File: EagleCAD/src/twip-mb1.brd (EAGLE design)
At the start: 81 x 88.9 mm, 13 parts, among them U1 GY-521MPU6050

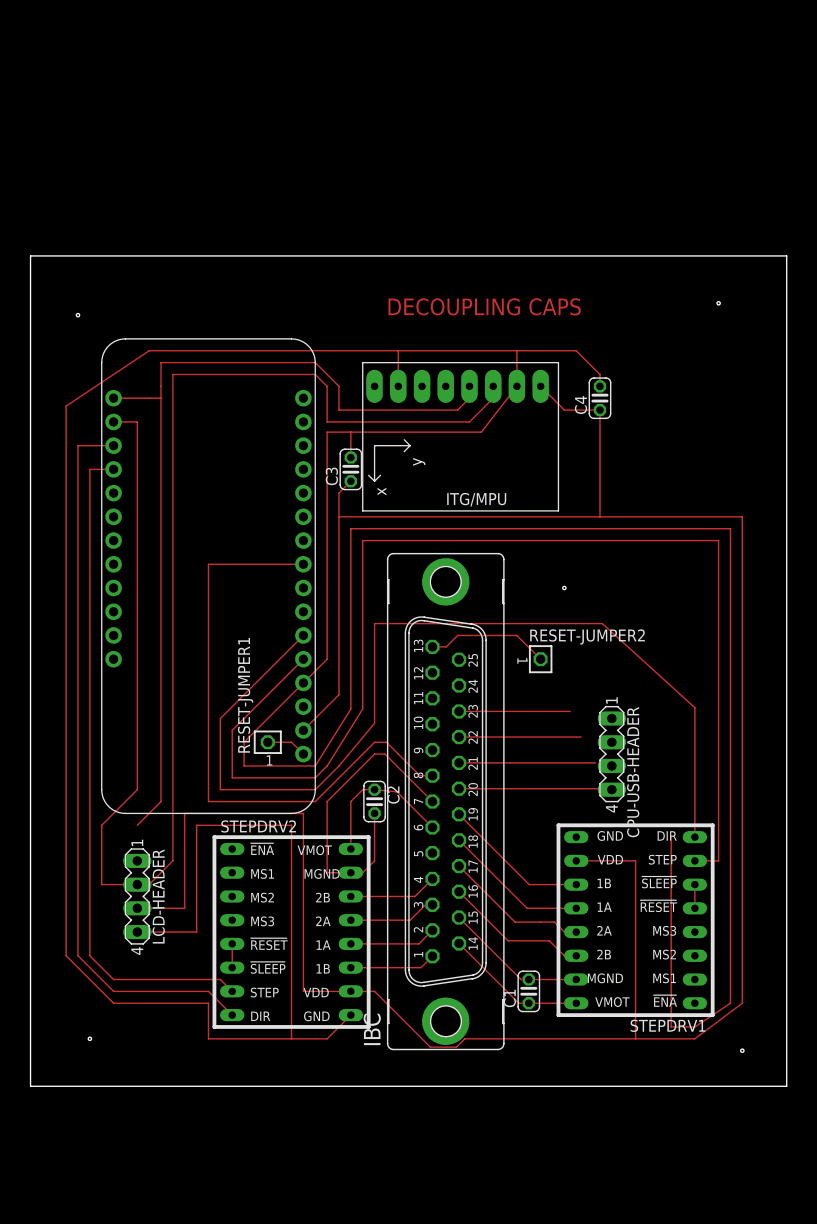
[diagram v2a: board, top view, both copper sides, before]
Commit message: minor layout fixes
need to use version numbers built into copper plate.
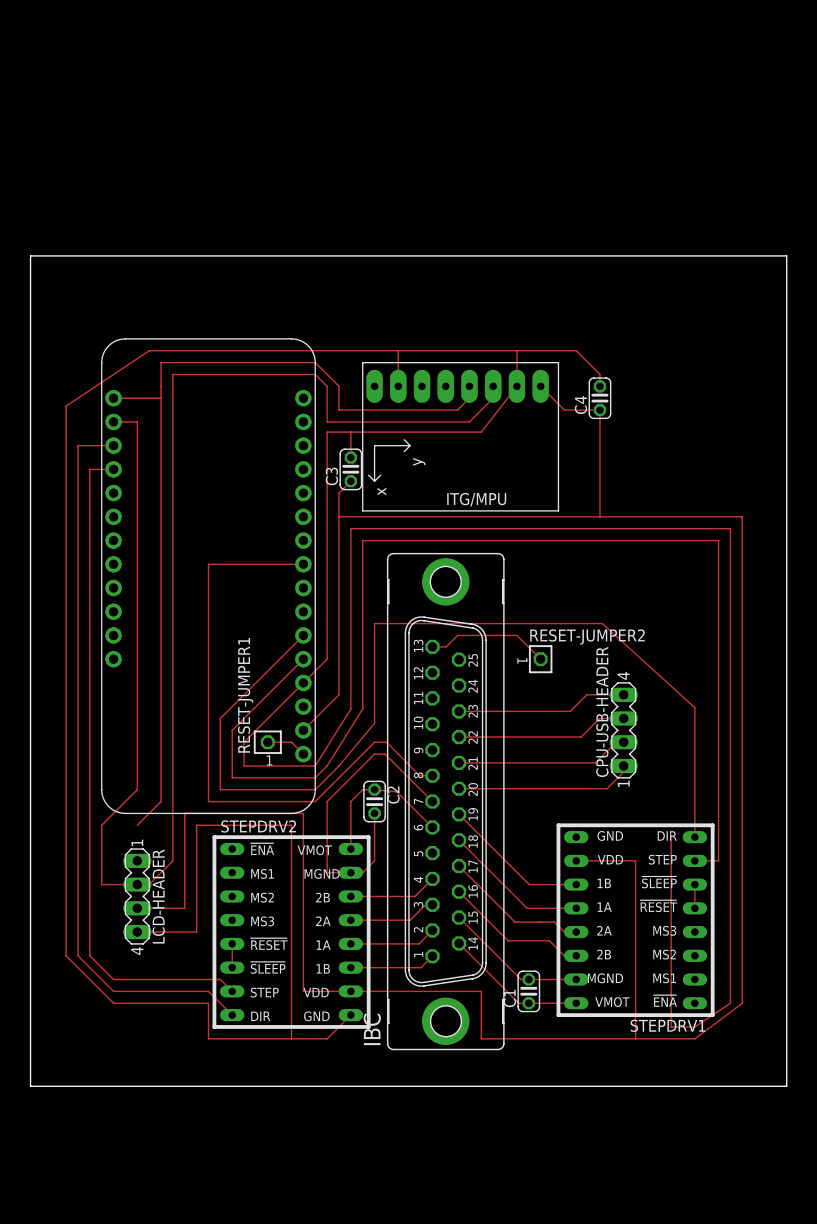
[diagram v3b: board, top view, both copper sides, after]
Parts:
- moved CPU-USB-HEADER 2.84 mm to (69.8, 38.1), turned to 90 degrees
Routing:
- net N$13: track 11.9 -> 18.4 mm
- net N$14: track 13.1 -> 18.4 mm
- net N$18: track 14.6 -> 18.5 mm
- net N$30: track 15.8 -> 19.0 mm
- net 3V: track 266.3 -> 268.6 mm
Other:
- board text removed: "DECOUPLING CAPS"
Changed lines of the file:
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@@
 <dimension x1="0" y1="0" x2="0" y2="88.9" x3="1.27" y3="44.45" textsize="1.778" layer="1" dtype="horizontal" unit="inch"/>
 <dimension x1="6.35" y1="-3.81" x2="87.63" y2="-5.08" x3="46.99" y3="-6.35" textsize="1.778" layer="1" dtype="horizontal" unit="inch"/>
-<hole x="11.43" y="82.55" drill="0.35"/>
-<hole x="80.01" y="83.82" drill="0.35"/>
-<hole x="63.5" y="53.34" drill="0.35"/>
-<hole x="12.7" y="5.08" drill="0.35"/>
-<hole x="82.55" y="3.81" drill="0.35"/>
-<text x="44.45" y="82.55" size="1.778" layer="1">DECOUPLING CAPS</text>
 </plain>
 <attributes>
@@
 <attribute name="SPICEPREFIX" value="C" x="43.18" y="30.48" size="1.778" layer="27" rot="R270" display="off"/>
 </element>
-<element name="CPU-USB-HEADER" library="con-lstb" library_urn="urn:adsk.eagle:library:162" package="MA04-1" package3d_urn="urn:adsk.eagle:package:8337/1" value="" x="68.58" y="35.56" rot="R270">
-<attribute name="MF" value="" x="68.58" y="35.56" size="1.778" layer="27" rot="R270" display="off"/>
-<attribute name="MPN" value="" x="68.58" y="35.56" size="1.778" layer="27" rot="R270" display="off"/>
-<attribute name="OC_FARNELL" value="unknown" x="68.58" y="35.56" size="1.778" layer="27" rot="R270" display="off"/>
-<attribute name="OC_NEWARK" value="unknown" x="68.58" y="35.56" size="1.778" layer="27" rot="R270" display="off"/>
+<element name="CPU-USB-HEADER" library="con-lstb" library_urn="urn:adsk.eagle:library:162" package="MA04-1" package3d_urn="urn:adsk.eagle:package:8337/1" value="" x="69.85" y="38.1" rot="R90">
+<attribute name="MF" value="" x="69.85" y="38.1" size="1.778" layer="27" rot="R90" display="off"/>
+<attribute name="MPN" value="" x="69.85" y="38.1" size="1.778" layer="27" rot="R90" display="off"/>
+<attribute name="OC_FARNELL" value="unknown" x="69.85" y="38.1" size="1.778" layer="27" rot="R90" display="off"/>
+<attribute name="OC_NEWARK" value="unknown" x="69.85" y="38.1" size="1.778" layer="27" rot="R90" display="off"/>
 </element>
 <element name="LCD-HEADER" library="con-lstb" library_urn="urn:adsk.eagle:library:162" package="MA04-1" package3d_urn="urn:adsk.eagle:package:8337/1" value="" x="17.78" y="20.32" rot="R270">
@@
 <wire x1="52.2224" y1="40.132" x2="64.124540625" y2="40.132" width="0.1524" layer="1"/>
 <contactref element="CPU-USB-HEADER" pad="4"/>
-<wire x1="64.124540625" y1="40.132" x2="68.58" y2="31.75" width="0" layer="19" extent="1-1"/>
+<wire x1="64.124540625" y1="40.132" x2="65.902540625" y2="41.91" width="0.1524" layer="1"/>
+<wire x1="65.902540625" y1="41.91" x2="69.85" y2="41.91" width="0.1524" layer="1"/>
 </signal>
 <signal name="N$14">
@@
 <wire x1="52.2224" y1="37.3888" x2="65.30254375" y2="37.3888" width="0.1524" layer="1"/>
 <contactref element="CPU-USB-HEADER" pad="3"/>
-<wire x1="65.30254375" y1="37.3888" x2="68.58" y2="34.29" width="0" layer="19" extent="1-1"/>
+<wire x1="65.30254375" y1="37.3888" x2="67.28374375" y2="39.37" width="0.1524" layer="1"/>
+<wire x1="67.28374375" y1="39.37" x2="69.85" y2="39.37" width="0.1524" layer="1"/>
 </signal>
 <signal name="N$18">
@@
 <wire x1="52.2224" y1="34.6202" x2="66.82481875" y2="34.6202" width="0.1524" layer="1"/>
 <contactref element="CPU-USB-HEADER" pad="2"/>
-<wire x1="66.82481875" y1="34.6202" x2="68.58" y2="36.83" width="0" layer="19" extent="1-1"/>
+<wire x1="66.82481875" y1="34.6202" x2="69.03461875" y2="36.83" width="0.1524" layer="1"/>
+<wire x1="69.03461875" y1="36.83" x2="69.85" y2="36.83" width="0.1524" layer="1"/>
 </signal>
 <signal name="N$30">
@@
 <wire x1="52.2224" y1="31.8516" x2="68.06474375" y2="31.8516" width="0.1524" layer="1"/>
 <contactref element="CPU-USB-HEADER" pad="1"/>
-<wire x1="68.06474375" y1="31.8516" x2="68.58" y2="39.37" width="0" layer="19" extent="1-1"/>
+<wire x1="68.06474375" y1="31.8516" x2="69.85" y2="33.63685625" width="0.1524" layer="1"/>
+<wire x1="69.85" y1="33.63685625" x2="69.85" y2="34.29" width="0.1524" layer="1"/>
 </signal>
 <signal name="N$35">
@@
 <wire x1="64.77" y1="24.13" x2="71.12" y2="24.13" width="0.1524" layer="1"/>
 <wire x1="77.47" y1="5.08" x2="71.12" y2="5.08" width="0.1524" layer="1"/>
-<wire x1="43.18" y1="10.16" x2="40.64" y2="10.16" width="0.1524" layer="1"/>
 <wire x1="39.37" y1="60.96" x2="67.31" y2="60.96" width="0.1524" layer="1"/>
 <wire x1="67.31" y1="60.96" x2="82.55" y2="60.96" width="0.1524" layer="1"/>
 <wire x1="77.47" y1="5.08" x2="82.55" y2="8.89" width="0.1524" layer="1"/>
 <wire x1="71.12" y1="24.13" x2="71.12" y2="5.08" width="0.1524" layer="1"/>
-<wire x1="71.12" y1="5.08" x2="52.83579375" y2="5.08" width="0.1524" layer="1"/>
-<wire x1="52.83579375" y1="5.08" x2="51.94679375" y2="4.191" width="0.1524" layer="1"/>
-<wire x1="51.94679375" y1="4.191" x2="49.149" y2="4.191" width="0.1524" layer="1"/>
-<wire x1="49.149" y1="4.191" x2="43.18" y2="10.16" width="0.1524" layer="1"/>
+<wire x1="71.12" y1="5.08" x2="54.61" y2="5.08" width="0.1524" layer="1"/>
 <contactref element="LCD-HEADER" pad="3"/>
 <wire x1="17.78" y1="19.05" x2="22.86" y2="19.05" width="0.1524" layer="1"/>
@@
 <wire x1="40.64" y1="64.77" x2="39.37" y2="63.5" width="0.1524" layer="1"/>
 <wire x1="39.37" y1="63.5" x2="39.37" y2="60.96" width="0.1524" layer="1"/>
+<wire x1="54.61" y1="10.16" x2="54.61" y2="5.08" width="0.1524" layer="1"/>
+<wire x1="40.64" y1="10.16" x2="54.61" y2="10.16" width="0.1524" layer="1"/>
 </signal>
 <signal name="N$1">

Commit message: minor fixes, and upsized boards to 3.3 x 5 inches
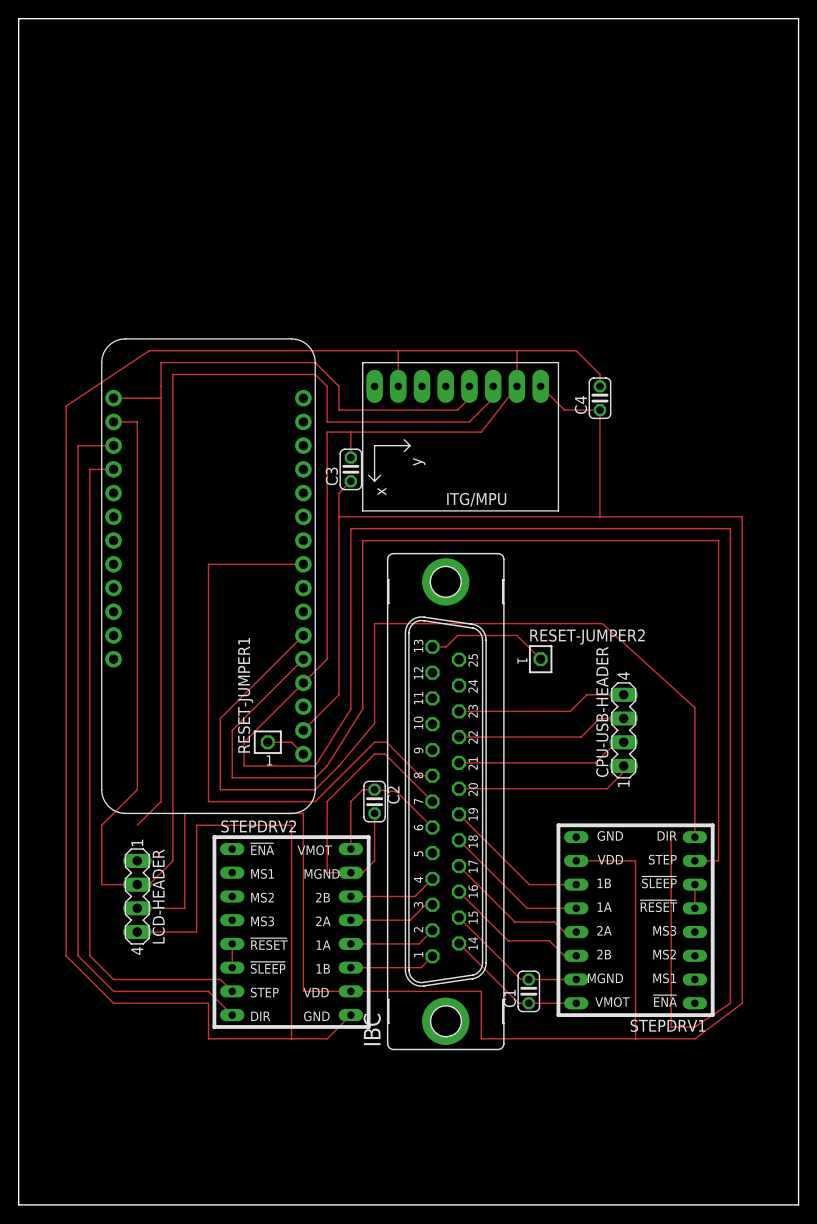
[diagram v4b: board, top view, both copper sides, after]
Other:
- board size 81 x 88.9 mm -> 83.5 x 127 mm
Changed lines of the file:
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@@
 <drawing>
 <settings>
-<setting alwaysvectorfont="no"/>
+<setting alwaysvectorfont="yes"/>
 <setting verticaltext="up"/>
 </settings>
-<grid distance="50" unitdist="mil" unit="mil" style="lines" multiple="1" display="no" altdistance="5" altunitdist="mil" altunit="mil"/>
+<grid distance="50" unitdist="mil" unit="mil" style="lines" multiple="10" display="yes" altdistance="5" altunitdist="mil" altunit="mil"/>
 <layers>
 <layer number="1" name="Top" color="4" fill="1" visible="yes" active="yes"/>
@@
 </layers>
 <board>
+<fusionsync huburn="a.cGVyc29uYWw6dWUyZDlmNmRl" projecturn="a.cGVyc29uYWw6dWUyZDlkNTAxIzIwMTgwODE4MTQ0NTE2MDUx" f3durn="urn:adsk.wipprod:dm.lineage:mZQQhy41S56UHTnbtTcFSg" pcbguid="5c8f9e4c-5e44-4e24-adda-79e9213756c3" lastpulledtime="" lastsyncedchangeguid="07d5f81c-c805-9028-98e1-ee9b7489bb23"/>
 <plain>
-<wire x1="6.35" y1="0" x2="87.3" y2="0" width="0" layer="20"/>
-<wire x1="87.3" y1="0" x2="87.3" y2="88.89" width="0" layer="20"/>
-<wire x1="87.3" y1="88.89" x2="6.35" y2="88.89" width="0" layer="20"/>
-<wire x1="6.35" y1="88.89" x2="6.35" y2="0" width="0" layer="20"/>
-<dimension x1="0" y1="0" x2="0" y2="88.9" x3="1.27" y3="44.45" textsize="1.778" layer="1" dtype="horizontal" unit="inch"/>
-<dimension x1="6.35" y1="-3.81" x2="87.63" y2="-5.08" x3="46.99" y3="-6.35" textsize="1.778" layer="1" dtype="horizontal" unit="inch"/>
+<wire x1="5.08" y1="-12.7" x2="88.57" y2="-12.7" width="0" layer="20"/>
+<wire x1="88.57" y1="-12.7" x2="88.57" y2="114.29" width="0" layer="20"/>
+<wire x1="88.57" y1="114.29" x2="5.08" y2="114.29" width="0" layer="20"/>
+<wire x1="5.08" y1="114.29" x2="5.08" y2="-12.7" width="0" layer="20"/>
+<dimension x1="88.9" y1="-5.08" x2="5.08" y2="-5.08" x3="46.99" y3="-17.78" textsize="1.778" layer="1" unit="inch"/>
+<dimension x1="-1.27" y1="114.3" x2="-1.27" y2="-12.7" x3="-2.54" y3="50.8" textsize="1.778" layer="1" unit="inch"/>
 </plain>
 <attributes>
@@
 </note>
 <note version="8.3" severity="warning">
+Since Version 8.3, EAGLE supports Fusion synchronisation.
+This feature will not be available in this version and saving
+the document will break the link to the Fusion PCB feature.
+</note>
+<note version="8.3" severity="warning">

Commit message: separate I2C buses with pullups
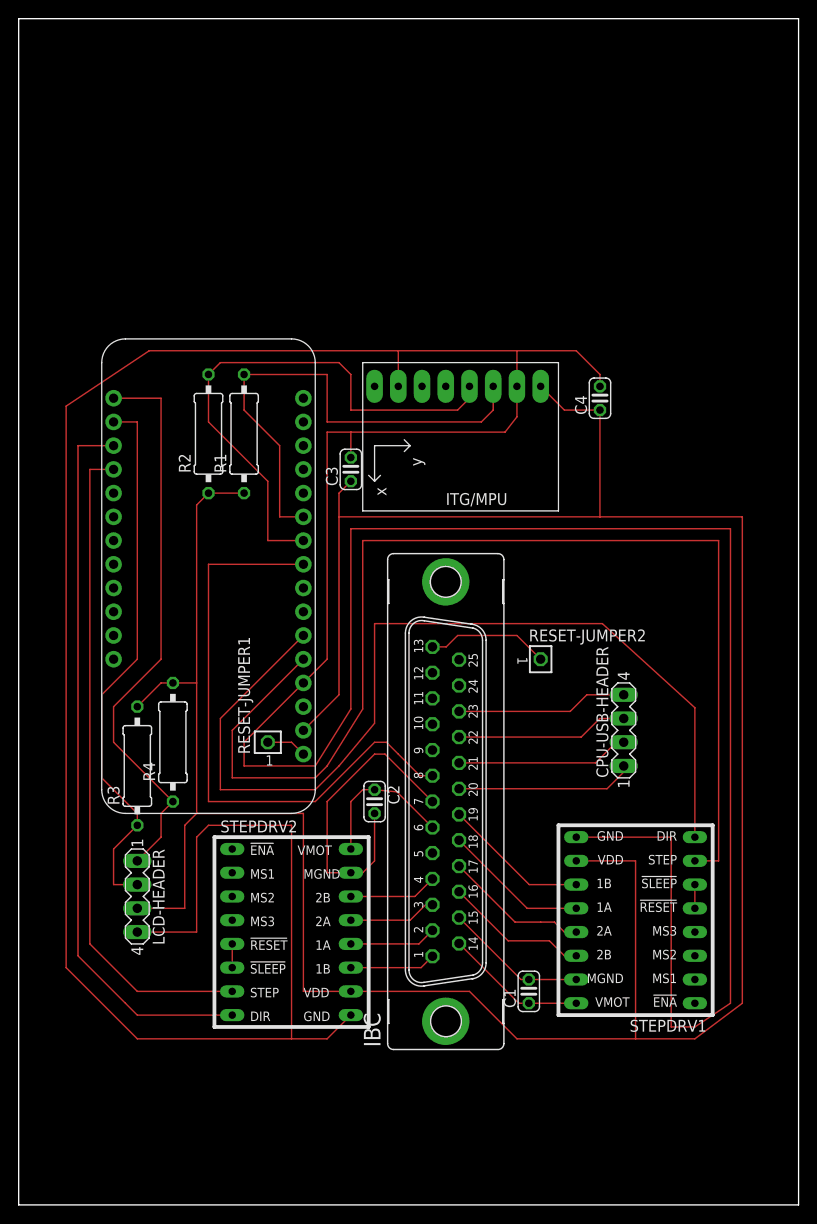
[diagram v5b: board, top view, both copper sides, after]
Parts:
- added R1, R2, R3, R4: 2K2, resistor:0309/12
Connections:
- new net N$17: MS2.11, R1.2, U1.SCL
- new net N$25: MS2.10, R2.2, U1.SDA
- net 3V: now also R1.1, R2.1, R3.2, R4.2
- net N$11: now also R3.1; no longer U1.SCL
- net N$19: now also R4.1; no longer U1.SDA
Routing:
- net N$11: track 155.3 -> 60.1 mm
- net N$25: track 0.00 -> 58.8 mm
- net N$17: track 0.00 -> 54.2 mm
- net 3V: track 268.6 -> 310.9 mm
- net N$19: track 94.1 -> 60.9 mm
- net N$35: track 433.8 -> 443.4 mm
- net N$29: track 71.4 -> 70.7 mm

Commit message: widen all traces from .006 to .012 inch
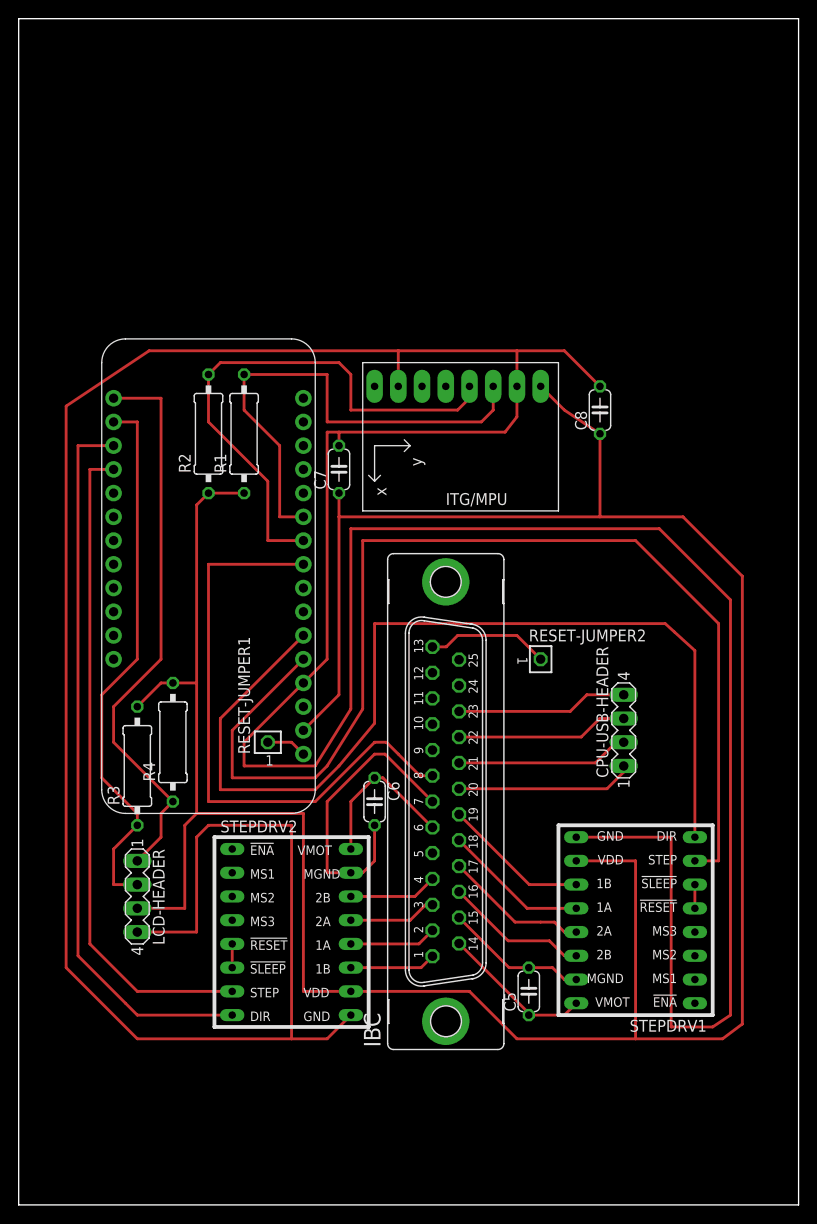
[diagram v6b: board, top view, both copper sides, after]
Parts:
- removed C1, C2, C3, C4: .1 uF, rcl:C025-024X044
- added C5, C6, C7, C8: (no value), rcl:C050-024X044
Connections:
- net 3V: now also C7.1, C8.1; no longer C3.1, C4.1
- net N$2: now also C6.2; no longer C2.2
- net N$20: now also C5.2; no longer C1.2
- net N$21: now also C6.1; no longer C2.1
- net N$22: now also C5.1; no longer C1.1
- net N$35: now also C7.2, C8.2; no longer C3.2, C4.2
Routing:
- net 3V: track 310.9 -> 305.1 mm
- net N$35: track 443.4 -> 437.8 mm
- net N$5: track 126.7 -> 121.5 mm
- net N$15: track 102.2 -> 105.9 mm
- net N$2: track 33.8 -> 32.5 mm
- net N$22: track 15.2 -> 16.4 mm
- net N$21: track 15.9 -> 17.1 mm
